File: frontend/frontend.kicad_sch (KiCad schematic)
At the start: 50 parts, among them Q1 T2N7002AK,LM, Q2 NX3008PBK,215, Q3 NX3008PBK,215, Q4 T2N7002AK,LM, Q5 NX3008PBK,215, Q6 T2N7002AK,LM, U1 ADS1291/2, U2 KC2016Z2

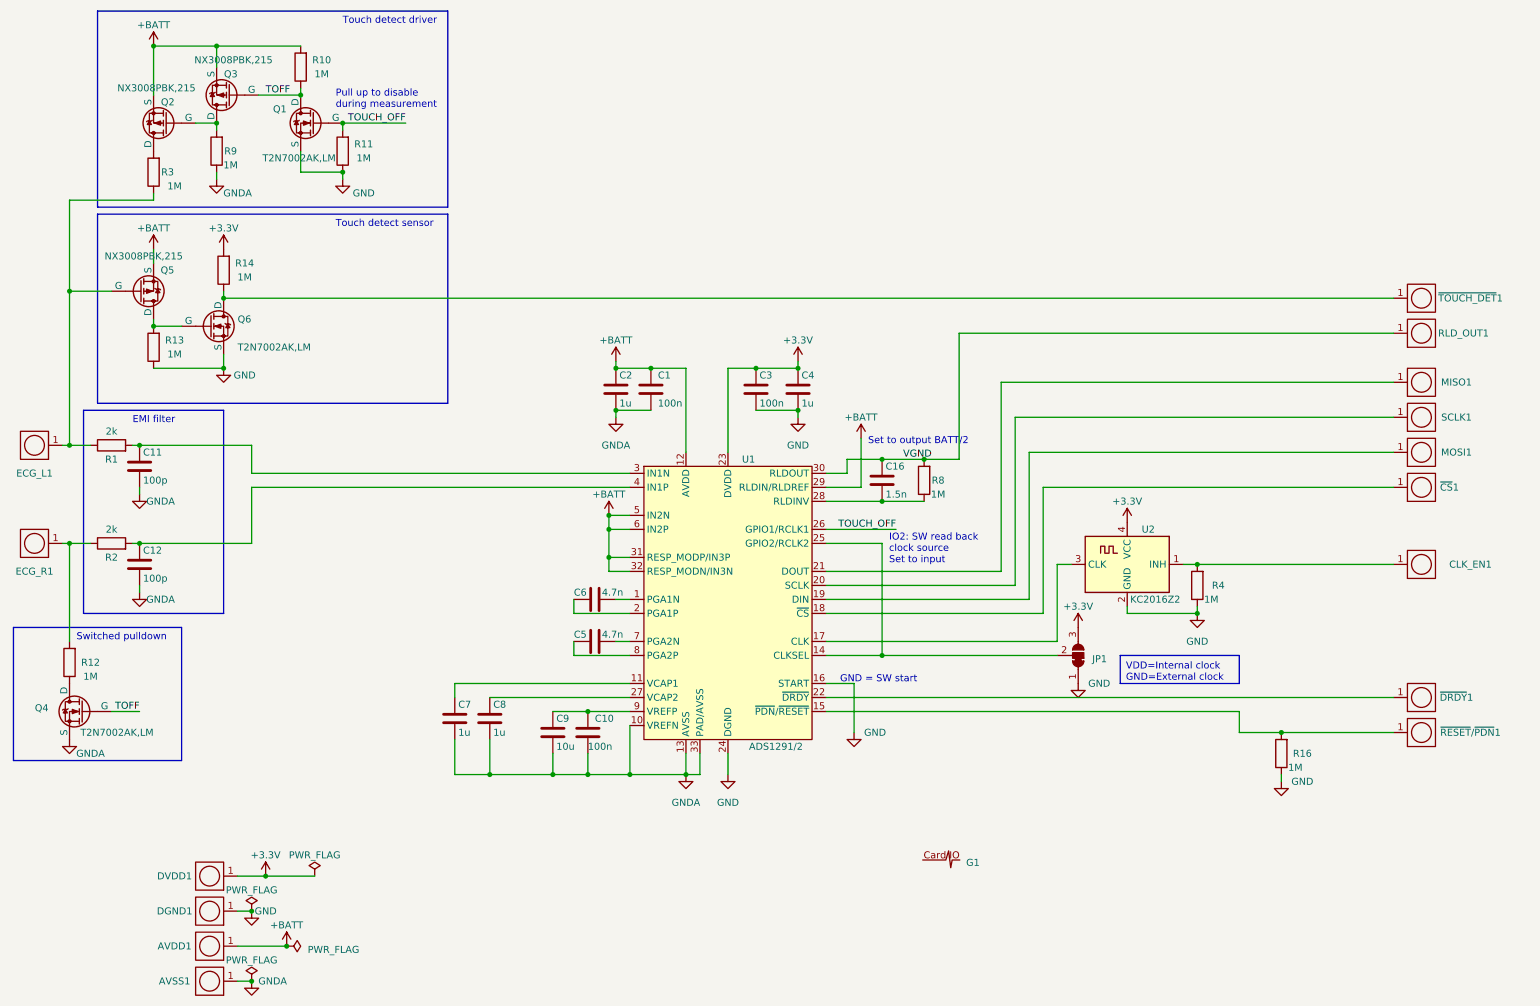
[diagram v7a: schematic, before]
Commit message: Add second channel components
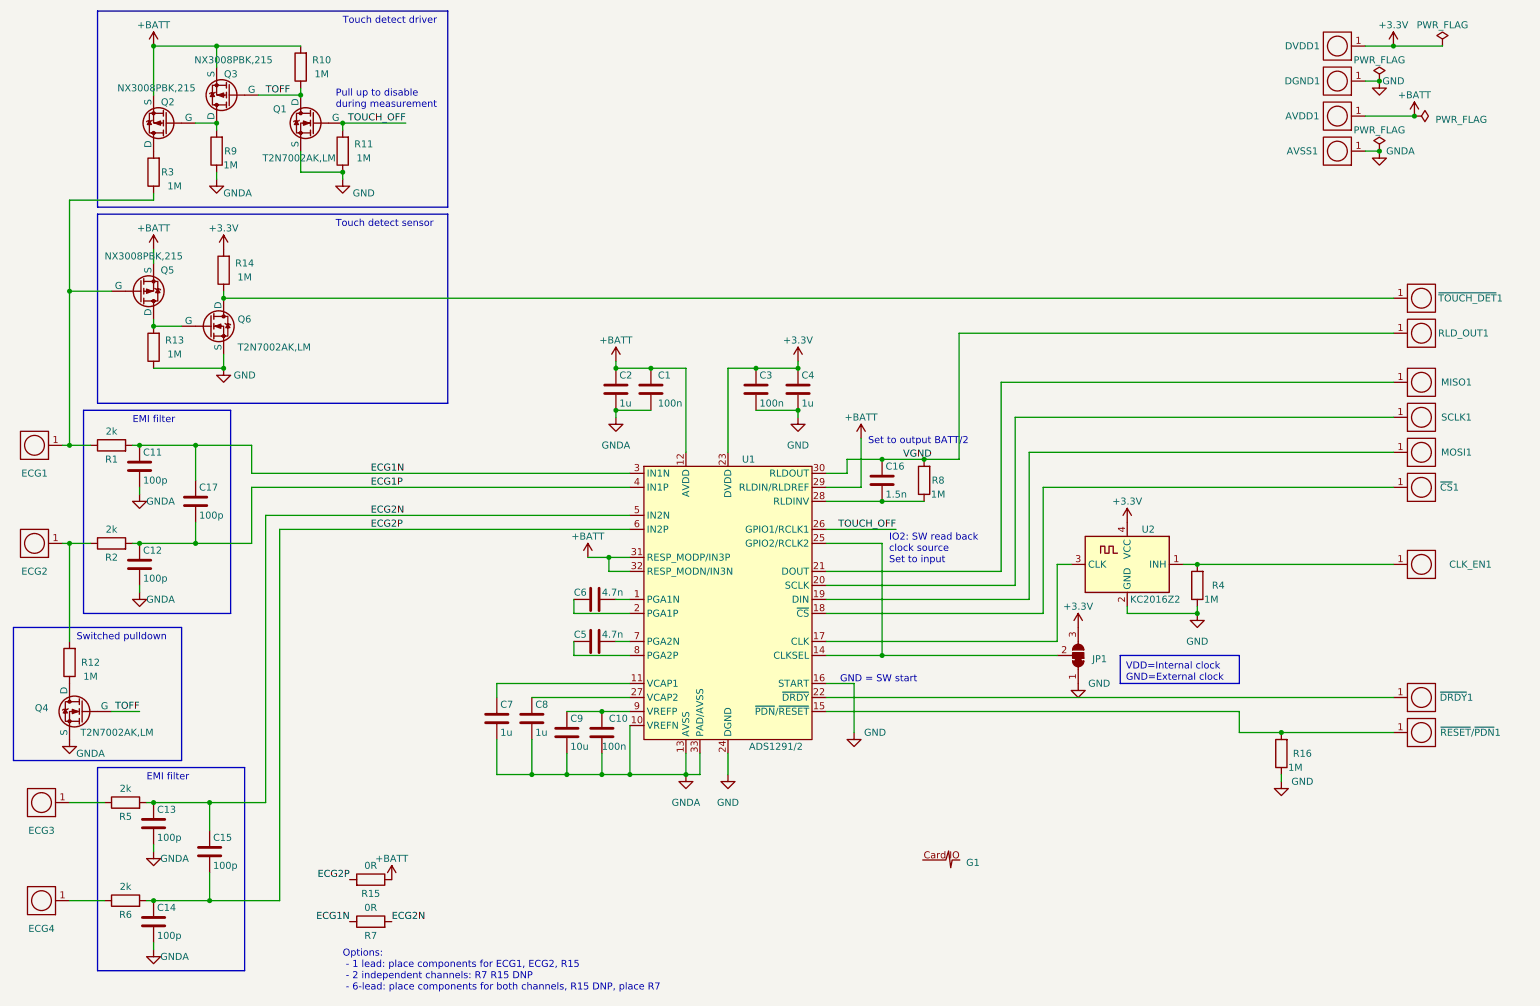
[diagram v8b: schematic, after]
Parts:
- added C13, C14, C15, C17: 100p, Capacitor_SMD:C_0603_1608Metric, symbol Device:C
- added ECG3, ECG4: ~, frontend_parts:PAD, symbol frontend_parts:PAD
- added R15, R7: 0R, Resistor_SMD:R_0603_1608Metric, symbol Device:R
- added R5, R6: 2k, Resistor_SMD:R_0603_1608Metric, symbol Device:R
- renumbered ECG_L1 to ECG1, ECG_R1 to ECG2
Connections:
- net +BATT: now also R15.1; no longer U1.5 (IN2N), U1.6 (IN2P)
- net GNDA: now also C13.2, C14.2
- net ECG1P: now reaches C12.1, R2.2, U1.4 (IN1P)
- net ECG1P: now also C17.2
- net ECG1N: now reaches C11.1, R1.2, U1.3 (IN1N)
- net ECG1N: now also C17.1, R7.1
- new net: ECG4.1, R6.1
- new net: ECG3.1, R5.1
- new net ECG2N: C13.1, C15.1, R5.2, R7.2, U1.5 (IN2N)
- new net ECG2P: C14.1, C15.2, R15.2, R6.2, U1.6 (IN2P)
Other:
- note added: "Options: - 1 lead: place components for ECG1, ECG2, R15 - 2 independent channels: R7 R15 DNP - 6-lead: place components for both channels, R15 DNP, place R7"
- moved on the sheet: AVDD1, AVSS1, C10, C7, C8, C9, DGND1, DVDD1
